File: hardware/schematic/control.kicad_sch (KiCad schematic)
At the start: 3 parts, among them SW3 BOOT / NO MOMENTARY, U1 Existing ESP32-S3, X1 RETAINED ASSEMBLY

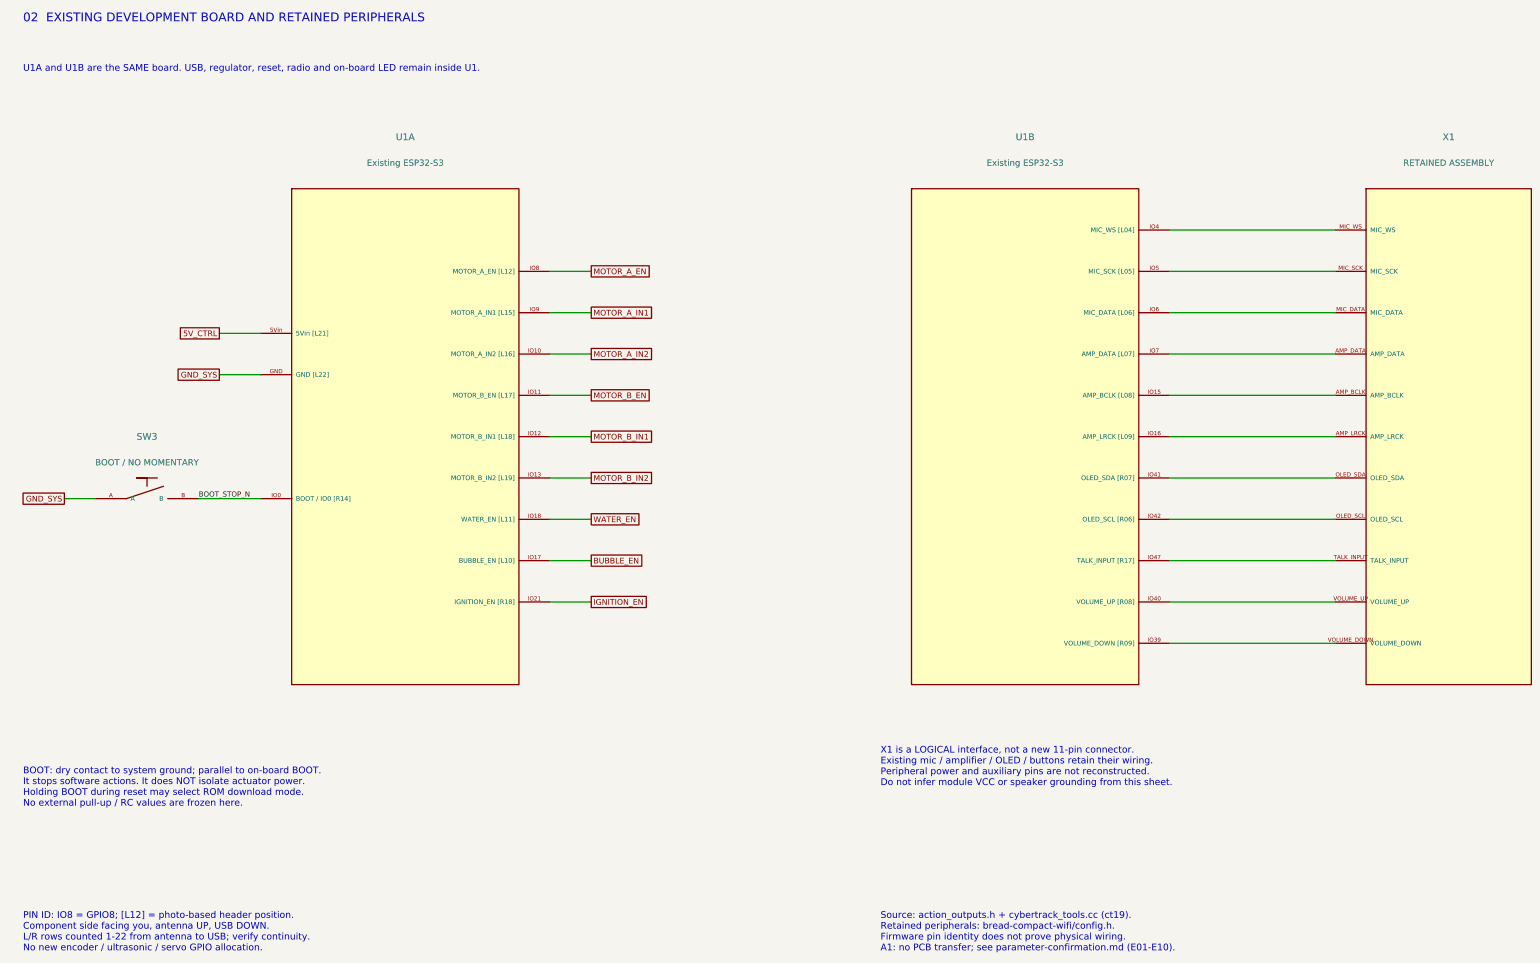
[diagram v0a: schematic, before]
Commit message: fix(schematic): add ultrasonic interface
Add controller 3V3, GPIO1 TRIG and GPIO2 ECHO on A2 sheet 6, and synchronize the current motor-side annotation and documentation.

Preserve A1 history and record fresh six-page exports, zero ERC violations, 112 connectivity checks and five regression tests.
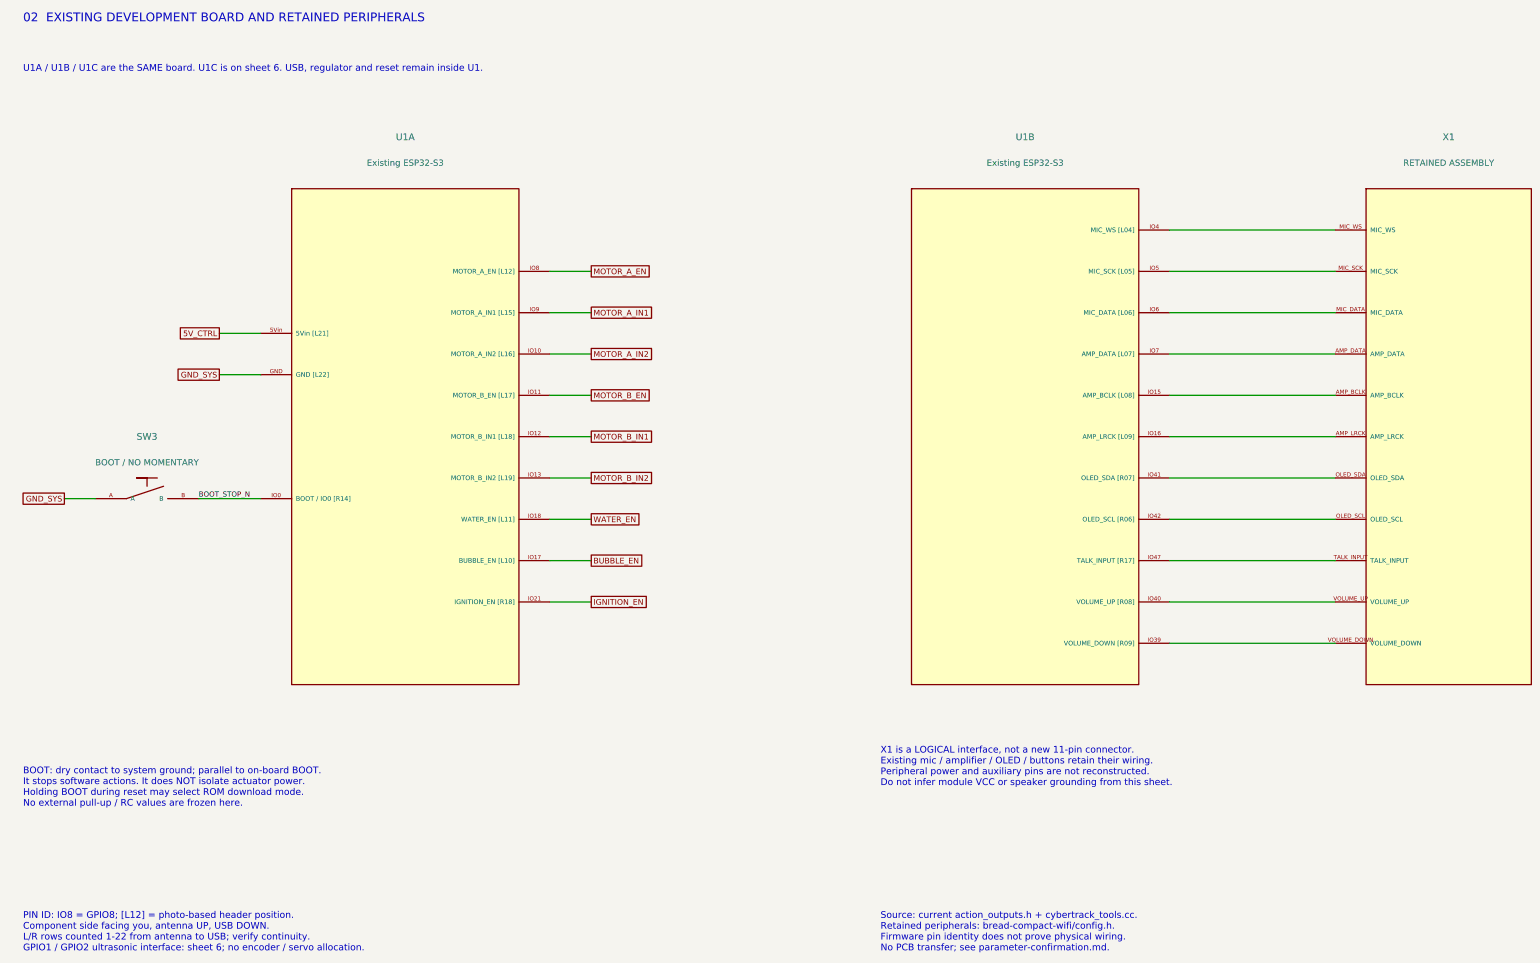
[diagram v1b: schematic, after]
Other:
- note added: "PIN ID: IO8 = GPIO8; [L12] = photo-based header position. Component side facing you, antenna UP, USB DOWN. L/R rows counted 1-22 from antenna to USB; verify continuity. GPIO1 / GPIO2 ultrasonic interface: sheet 6; no encoder / servo allocation."
- note added: "Source: current action_outputs.h + cybertrack_tools.cc. Retained peripherals: bread-compact-wifi/config.h. Firmware pin identity does not prove physical wiring. No PCB transfer; see parameter-confirmation.md."
- note added: "U1A / U1B / U1C are the SAME board. U1C is on sheet 6. USB, regulator and reset remain inside U1."
- note removed: "PIN ID: IO8 = GPIO8; [L12] = photo-based header position. Component side facing you, antenna UP, USB DOWN. L/R rows counted 1-22 from antenna to USB; verify continuity. No new encoder / ultrasonic / servo GPIO allocation."
- note removed: "Source: action_outputs.h + cybertrack_tools.cc (ct19). Retained peripherals: bread-compact-wifi/config.h. Firmware pin identity does not prove physical wiring. A1: no PCB transfer; see parameter-confirmation.md (E01-E10)."
- note removed: "U1A and U1B are the SAME board. USB, regulator, reset, radio and on-board LED remain inside U1."
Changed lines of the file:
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@@
-(kicad_sch (version 20250114) (generator "cybertrack_schematic") (paper "A3") (title_block (title "CyberTrack / ESP32-S3 and BOOT") (date "2026-10-26") (rev "A1") (company "CyberTrack") (comment 1 "MODULE INTERCONNECTION SCHEMATIC - NOT FOR FABRICATION") (comment 2 "Retain existing ESP32-S3 board; TBD items are unresolved") (comment 3 "Pin IDs identify signals, NOT physical header positions"))
+(kicad_sch (version 20250114) (generator "cybertrack_schematic") (paper "A3") (title_block (title "CyberTrack / ESP32-S3 and BOOT") (date "2026-10-30") (rev "A2") (company "CyberTrack") (comment 1 "MODULE INTERCONNECTION SCHEMATIC - NOT FOR FABRICATION") (comment 2 "Retain existing ESP32-S3 board; TBD items are unresolved") (comment 3 "Pin IDs identify signals, NOT physical header positions"))
 (text "02  EXISTING DEVELOPMENT BOARD AND RETAINED PERIPHERALS" (at 20.32 17.78 0) (effects (font (size 2.159 2.159)) (justify left top)))
-(text "U1A and U1B are the SAME board. USB, regulator, reset, radio and on-board LED remain inside U1." (at 20.32 30.48 0) (effects (font (size 1.651 1.651)) (justify left top)))
+(text "U1A / U1B / U1C are the SAME board. U1C is on sheet 6. USB, regulator and reset remain inside U1." (at 20.32 30.48 0) (effects (font (size 1.651 1.651)) (justify left top)))
 (symbol (lib_id "CyberTrack:Existing_ESP32S3") (at 114.3 121.92 0) (unit 1) (in_bom no) (on_board no) (dnp no)(property "Reference" "U1" (at 114.3 48.26 0) (effects (font (size 1.651 1.651))))
 (property "Value" "Existing ESP32-S3" (at 114.3 54.61 0) (effects (font (size 1.524 1.524))))
@@
 (text "X1 is a LOGICAL interface, not a new 11-pin connector.\nExisting mic / amplifier / OLED / buttons retain their wiring.\nPeripheral power and auxiliary pins are not reconstructed.\nDo not infer module VCC or speaker grounding from this sheet." (at 231.14 198.12 0) (effects (font (size 1.651 1.651)) (justify left top)))
 (text "BOOT: dry contact to system ground; parallel to on-board BOOT.\nIt stops software actions. It does NOT isolate actuator power.\nHolding BOOT during reset may select ROM download mode.\nNo external pull-up / RC values are frozen here." (at 20.32 203.2 0) (effects (font (size 1.651 1.651)) (justify left top)))
-(text "PIN ID: IO8 = GPIO8; [L12] = photo-based header position.\nComponent side facing you, antenna UP, USB DOWN.\nL/R rows counted 1-22 from antenna to USB; verify continuity.\nNo new encoder / ultrasonic / servo GPIO allocation." (at 20.32 238.76 0) (effects (font (size 1.651 1.651)) (justify left top)))
-(text "Source: action_outputs.h + cybertrack_tools.cc (ct19).\nRetained peripherals: bread-compact-wifi/config.h.\nFirmware pin identity does not prove physical wiring.\nA1: no PCB transfer; see parameter-confirmation.md (E01-E10)." (at 231.14 238.76 0) (effects (font (size 1.651 1.651)) (justify left top)))
+(text "PIN ID: IO8 = GPIO8; [L12] = photo-based header position.\nComponent side facing you, antenna UP, USB DOWN.\nL/R rows counted 1-22 from antenna to USB; verify continuity.\nGPIO1 / GPIO2 ultrasonic interface: sheet 6; no encoder / servo allocation." (at 20.32 238.76 0) (effects (font (size 1.651 1.651)) (justify left top)))
+(text "Source: current action_outputs.h + cybertrack_tools.cc.\nRetained peripherals: bread-compact-wifi/config.h.\nFirmware pin identity does not prove physical wiring.\nNo PCB transfer; see parameter-confirmation.md." (at 231.14 238.76 0) (effects (font (size 1.651 1.651)) (justify left top)))
 )
